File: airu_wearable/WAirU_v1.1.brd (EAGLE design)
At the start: 43.8 x 51.7 mm, 50 parts, among them Q2 MMBT3904LT1G, Q3 MMBT3904LT1G, Q6 BSS84, U2 CN3065-DFN8, U3 HDC1080DMBT, U4 PAM2305AABADJ, U6 PAM2401, U7 ESP32_WROOM32_SKINNY

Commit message: an airwire
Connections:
- new net N$7: U7.16
- net GP_LED: now also U7.33; no longer U7.16
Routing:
- net 3.3V: track 118.0 -> 118.6 mm
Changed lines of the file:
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@@
 <wire x1="28.2575" y1="0.9525" x2="28.280025" y2="1.01589375" width="0.1524" layer="1"/>
 <wire x1="26.3525" y1="0.3175" x2="26.27469375" y2="0.16931875" width="0.1524" layer="1"/>
-<wire x1="26.3525" y1="0.9525" x2="26.3525" y2="1.905" width="0.1524" layer="1"/>
 <wire x1="20.8026" y1="2.7406625" x2="20.06886875" y2="2.00693125" width="0.1524" layer="1"/>
 <wire x1="24.765" y1="2.8575" x2="24.638" y2="2.7305" width="0.1524" layer="16"/>
@@
 <wire x1="21.1353375" y1="2.7406625" x2="18.415" y2="5.461" width="0.1524" layer="16"/>
 <wire x1="18.415" y1="5.461" x2="18.415" y2="6.35" width="0.1524" layer="16"/>
-<wire x1="25.4" y1="3.175" x2="26.3525" y2="2.2225" width="0.1524" layer="1"/>
+<wire x1="26.3525" y1="2.2225" x2="25.4" y2="3.175" width="0.1524" layer="1"/>
 <wire x1="25.4" y1="3.4925" x2="25.4" y2="3.175" width="0.1524" layer="1"/>
 <wire x1="25.143165625" y1="3.235665625" x2="25.463459375" y2="4.394609375" width="0.1524" layer="1"/>
@@
 <wire x1="33.9725" y1="2.8575" x2="34.6075" y2="2.2225" width="0.1524" layer="1"/>
 <wire x1="26.67" y1="2.8575" x2="33.9725" y2="2.8575" width="0.1524" layer="1"/>
-<wire x1="26.67" y1="2.2225" x2="26.67" y2="2.8575" width="0.1524" layer="1"/>
+<wire x1="26.67" y1="2.8575" x2="26.67" y2="2.2225" width="0.1524" layer="1"/>
 <via x="20.8026" y="2.7406625" extent="1-16" drill="0.254"/>
 <via x="24.765" y="2.8575" extent="1-16" drill="0.254"/>
@@
 <wire x1="13.65758125" y1="37.92651875" x2="13.65758125" y2="36.5125" width="0.1524" layer="1"/>
 <contactref element="R5" pad="2"/>
+<wire x1="26.3525" y1="0.9525" x2="26.3525" y2="2.2225" width="0.1524" layer="1"/>
+<wire x1="26.67" y1="2.2225" x2="26.3525" y2="2.2225" width="0.1524" layer="1"/>
 <wire x1="19.621884375" y1="1.797278125" x2="0.396240625" y2="-43.933615625" width="0" layer="19" extent="1-1"/>
-<wire x1="26.3525" y1="1.905" x2="26.3525" y2="2.2225" width="0" layer="19" extent="1-1"/>
-<wire x1="26.67" y1="2.2225" x2="26.3525" y2="2.2225" width="0" layer="19" extent="1-1"/>
 </signal>
 <signal name="RESET">
@@
 <signal name="GP_LED">
 <contactref element="U$4" pad="1"/>
-<contactref element="U7" pad="16"/>
-<wire x1="3.4021" y1="-44.17271875" x2="26.5959625" y2="24.41608125" width="0" layer="19" extent="1-1"/>
+<contactref element="U7" pad="33"/>
+<wire x1="3.4021" y1="-44.17271875" x2="39.5259625" y2="35.96608125" width="0" layer="19" extent="1-1"/>
 </signal>
 <signal name="CHARGING">
@@
 <wire x1="0.396240625" y1="-42.517821875" x2="4.8021" y2="-44.17271875" width="0" layer="19" extent="1-1"/>
 </signal>
+<signal name="N$7">
+<contactref element="U7" pad="16"/>
+</signal>
 </signals>

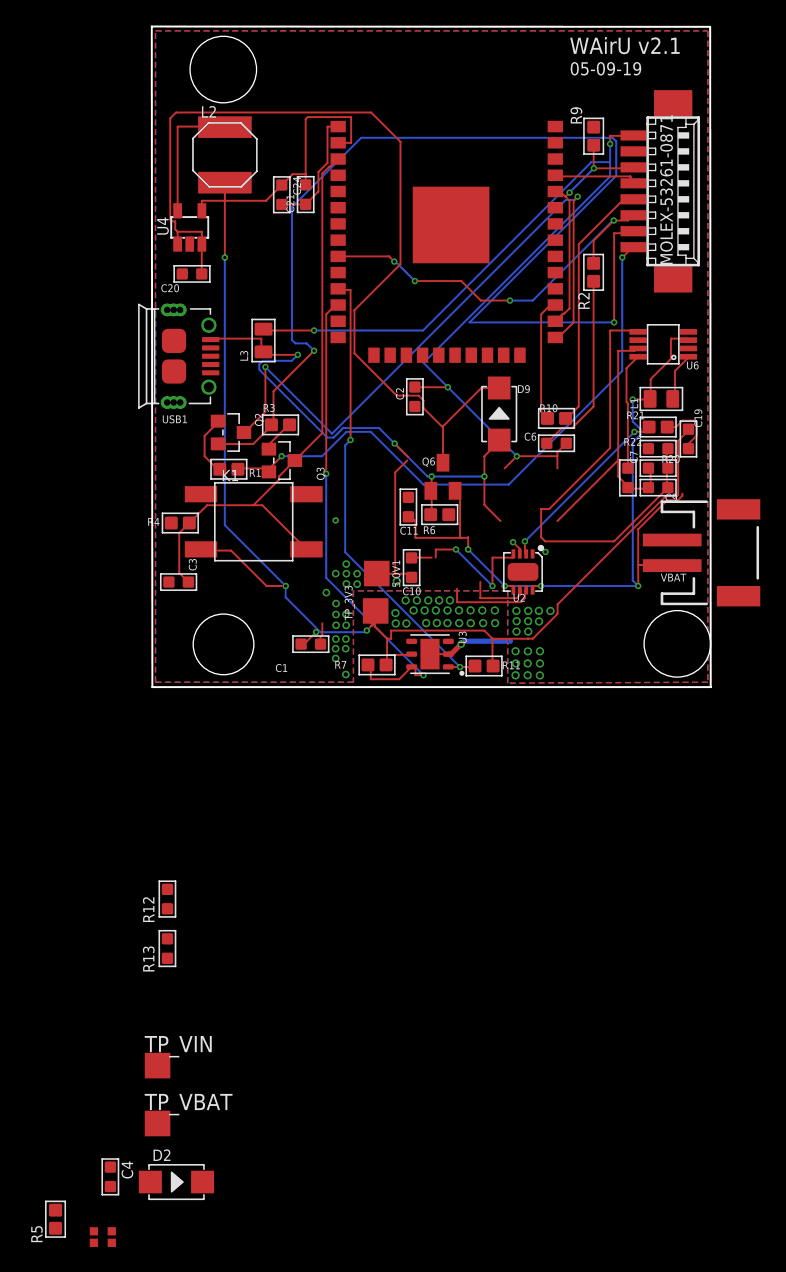
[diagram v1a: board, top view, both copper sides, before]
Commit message: Apply changes in schematic to PCB
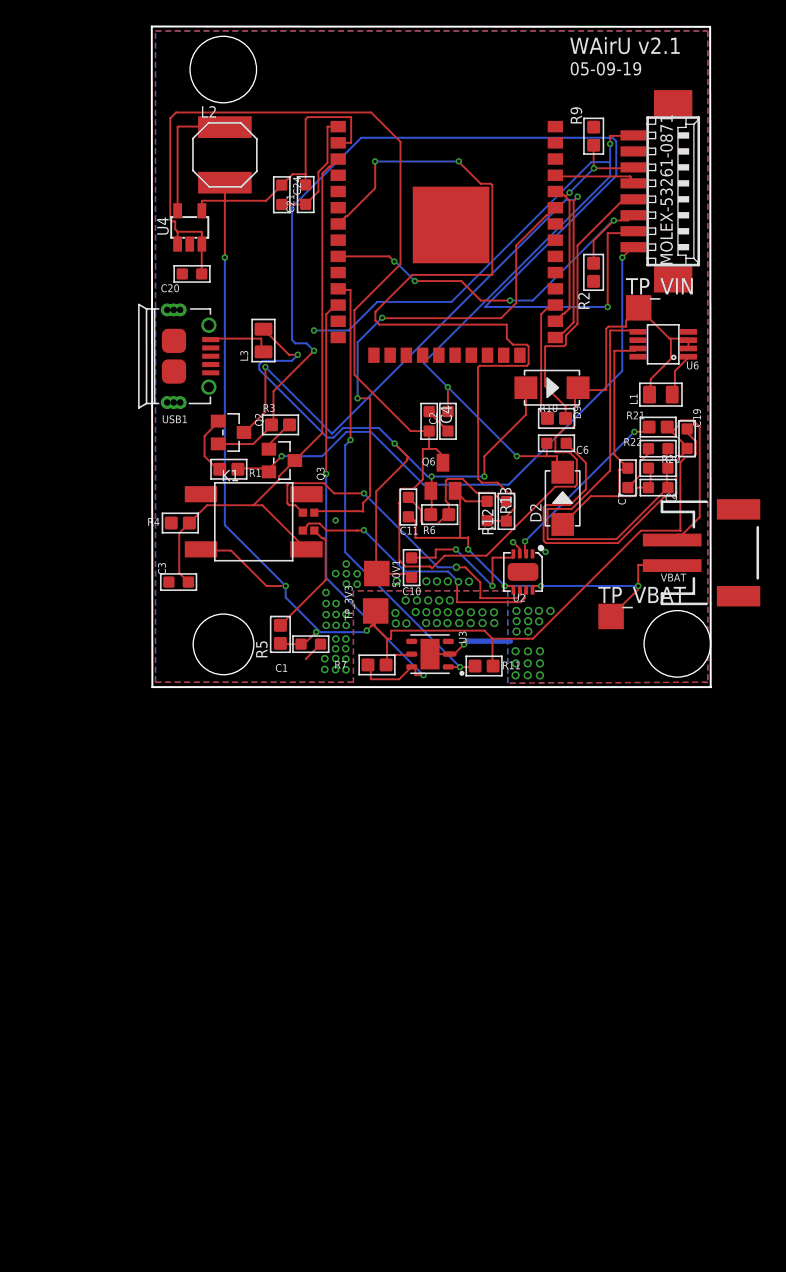
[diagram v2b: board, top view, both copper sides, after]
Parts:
- moved TP_VIN 70.3 mm to (46.1, 28.1)
- moved C4 64.2 mm to (29.6, 19.2)
- moved D2 61.5 mm to (40.1, 13.2), turned to 90 degrees
- moved U$4 58.3 mm to (20.2, 11.4), turned to 270 degrees
- moved TP_VBAT 53.3 mm to (43.9, 3.96)
- moved R5 49.1 mm to (18.0, 2.56)
- moved R13 42.4 mm to (34.2, 12.2), turned to 180 degrees
- moved R12 40.3 mm to (35.7, 12.2)
- moved D9 4.62 mm to (39.3, 21.9), turned to 0 degrees
- moved C2 3.22 mm to (31.1, 19.2)
- moved L1 0.34 mm to (47.8, 21.3)
- moved C19 0.11 mm to (49.8, 17.9)
- turned C6 to 270 degrees
- turned C7 to 180 degrees
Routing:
- net BAT_CHECK: track 0.00 -> 69.1 mm, vias 0 -> 2
- net V_IN: track 77.7 -> 124.1 mm
- net GP_LED: track 0.00 -> 40.9 mm, vias 0 -> 2
- net GND: track 48.2 -> 81.2 mm
- net CHG_DONE: track 4.98 -> 26.3 mm, vias 0 -> 2
- net VBAT: track 55.7 -> 37.8 mm, vias 5 -> 4
- net CHARGING: track 7.22 -> 22.2 mm, vias 0 -> 2
- net N$9: track 0.00 -> 9.34 mm
- net 5.0V: track 78.1 -> 72.1 mm
- net 3.3V: track 118.6 -> 122.8 mm
- net DTR: track 91.1 -> 87.0 mm
- net VBUS: track 52.5 -> 55.6 mm
- net TXD: track 19.8 -> 22.3 mm
- net N$4: track 22.7 -> 24.7 mm

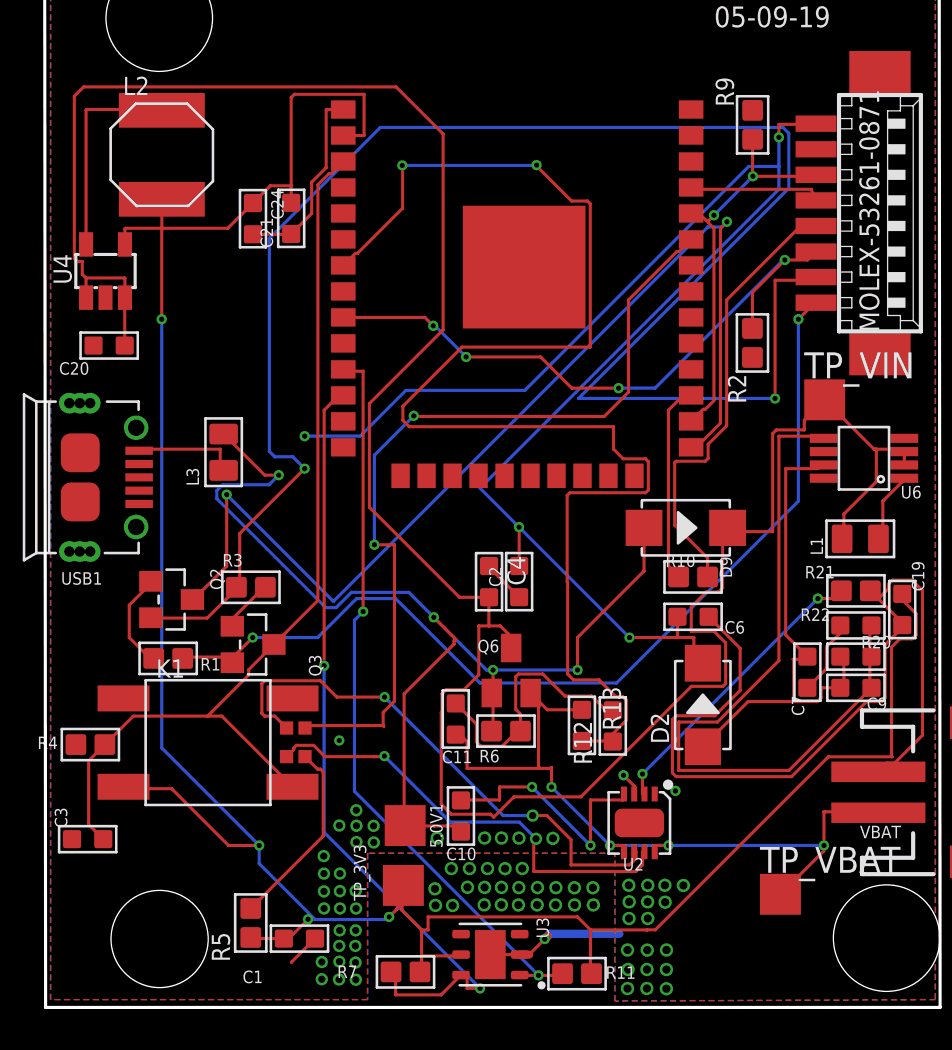
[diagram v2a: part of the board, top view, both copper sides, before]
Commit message: removed old directories
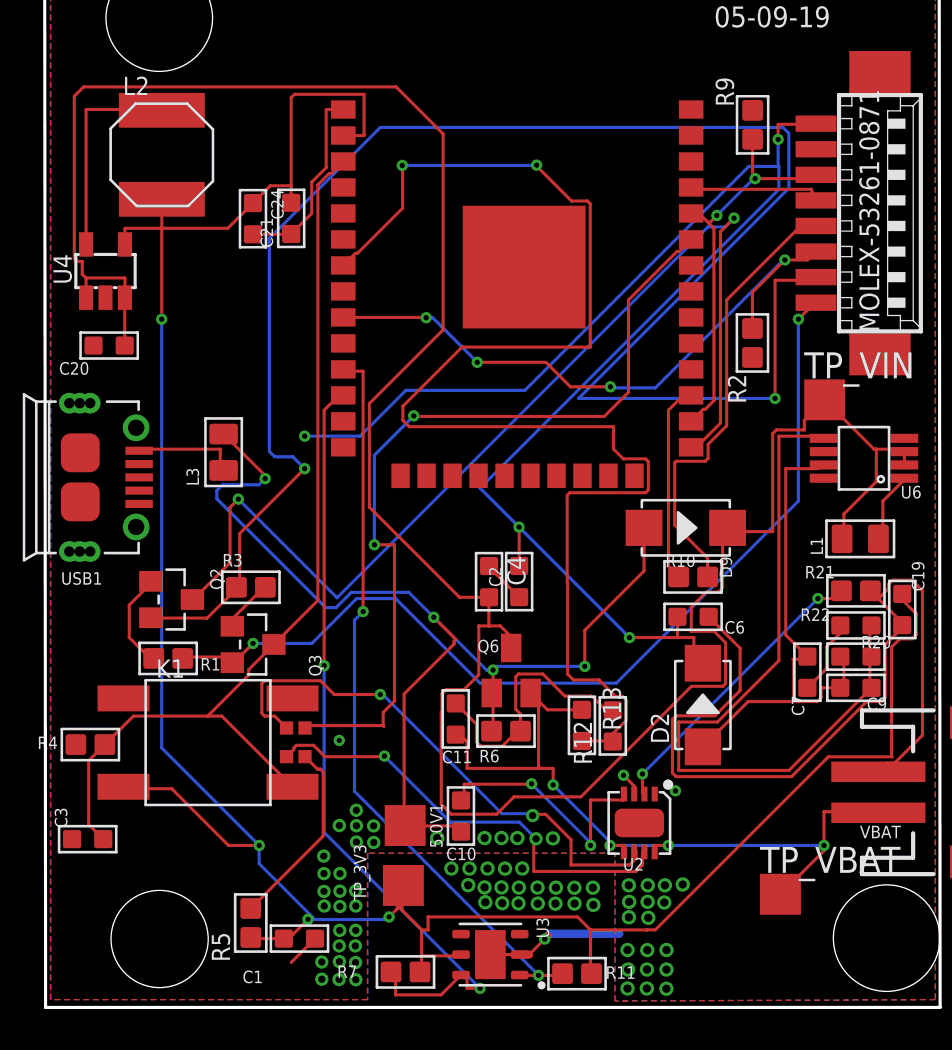
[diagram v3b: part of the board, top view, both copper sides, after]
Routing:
- net VBUS: track 55.6 -> 54.5 mm
